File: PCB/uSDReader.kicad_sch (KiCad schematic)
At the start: 30 parts, among them IC1 USB2244I-AEZG-06-TR, J1 Micro_SD_Card_Det1, J2 USB_A, U1 LM1117MP-3.3, Y2 Crystal 24MHz (±350 ppm)

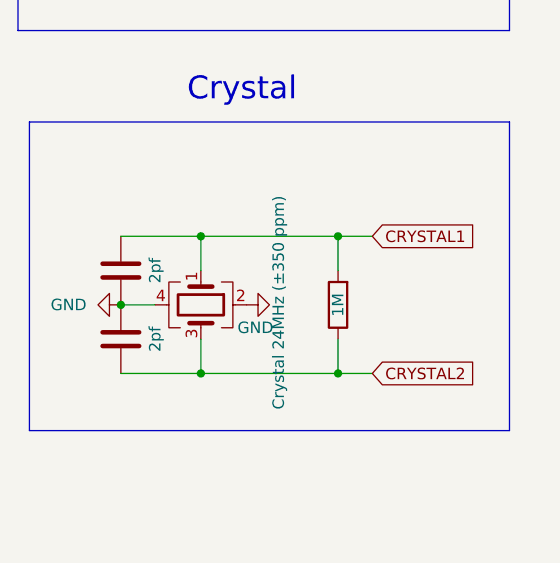
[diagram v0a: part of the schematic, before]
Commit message: REV 4
Swapped the voltage regulator and the status LED and cleaned up traces
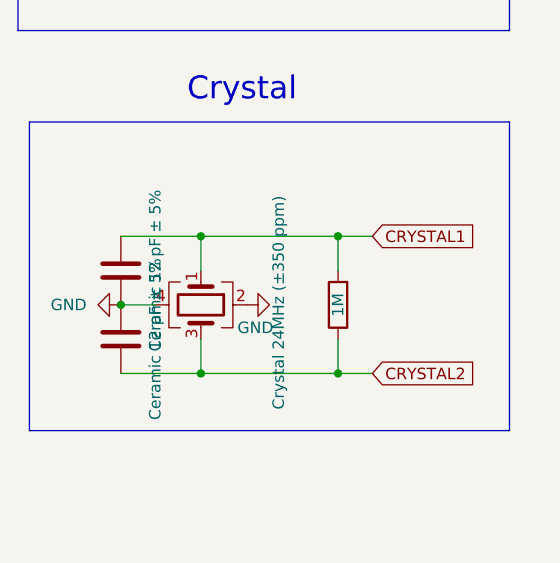
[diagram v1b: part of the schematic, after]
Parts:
- C11, C12: value 2pf -> Ceramic 12 pF ± 5%
- D1: JLCPCB Part (none) -> C5182099
- J1: JLCPCB Part (none) -> C113206
- J2: JLCPCB Part (none) -> C5393
- Y2: JLCPCB Part (none) -> C2965580
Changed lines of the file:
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@@
+			)
+		)
+		(property "JLCPCB Part" "C5182099"
+			(at 67.31 67.31 90)
+			(effects
+				(font
+					(size 1.27 1.27)
+				)
+				(hide yes)
 			)
 		)
@@
 			)
 		)
-		(property "Value" "2pf"
+		(property "Value" "Ceramic 12 pF ± 5%"
 			(at 54.61 129.54 90)
 			(effects
@@
 			)
 		)
+		(property "JLCPCB Part" "C5393"
+			(at 54.61 44.45 0)
+			(effects
+				(font
+					(size 1.27 1.27)
+				)
+				(hide yes)
+			)
+		)
 		(pin "2"
 		)
@@
 			)
 		)
-		(property "Value" "2pf"
+		(property "Value" "Ceramic 12 pF ± 5%"
 			(at 54.61 121.92 90)
 			(effects
@@
 			)
 		)
+		(property "JLCPCB Part" "C113206"
+			(at 243.84 90.17 0)
+			(effects
+				(font
+					(size 1.27 1.27)
+				)
+				(hide yes)
+			)
+		)
 		(pin "7"
 		)
@@
 			(at 59.69 125.73 0)
 			(effects
+				(font
+					(size 1.27 1.27)
+				)
+				(hide yes)
+			)
+		)
+		(property "JLCPCB Part" "C2965580"
+			(at 59.69 125.73 0)
+			(effects
